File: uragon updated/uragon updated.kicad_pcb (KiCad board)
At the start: 4 copper layers, 89.7 x 62 mm, 70 parts, among them J1 USB_C_Receptacle_USB2.0_16P, J10 Conn_01x02_Socket, J11 01x07, J2 Conn_01x16_Socket, J3 Conn_01x16_Socket, J4 Conn_01x02_Socket, J5 01x07, J6 01x03, J7 01x03, J8 01x04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

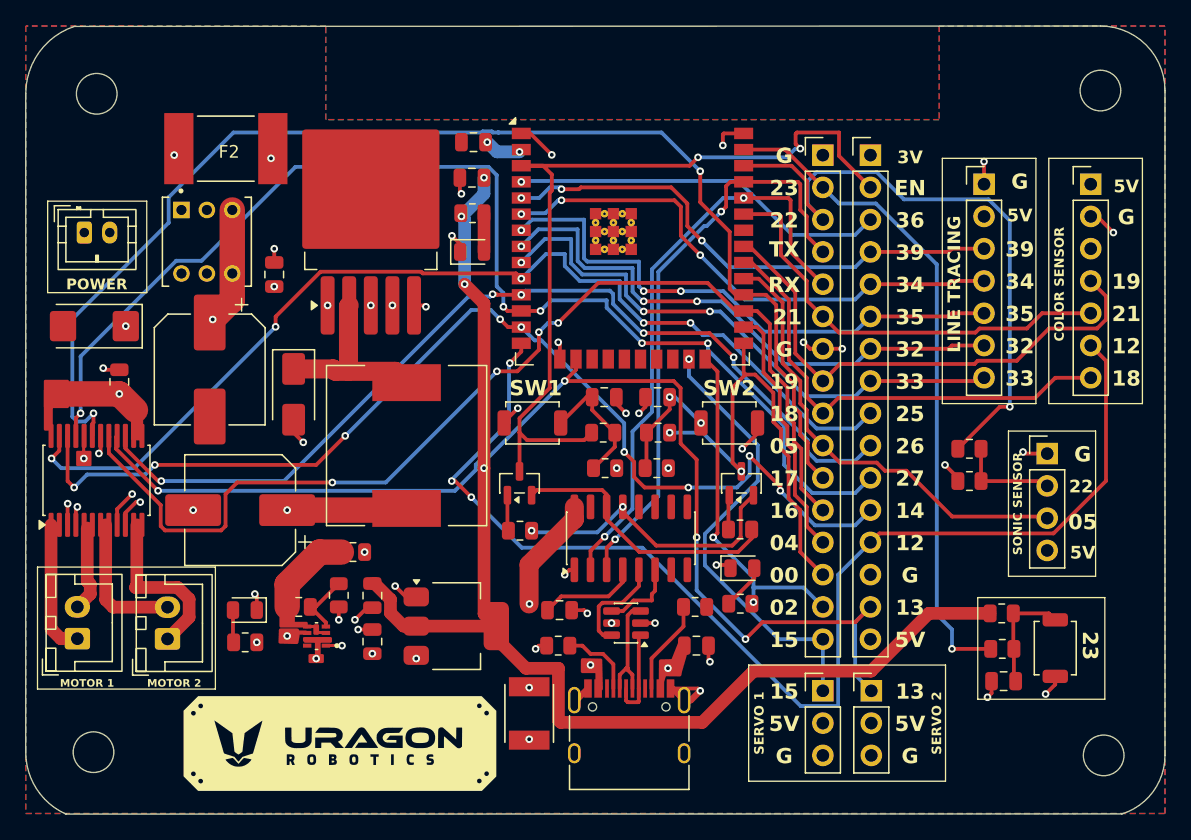
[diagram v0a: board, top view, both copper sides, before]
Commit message: Added diodes
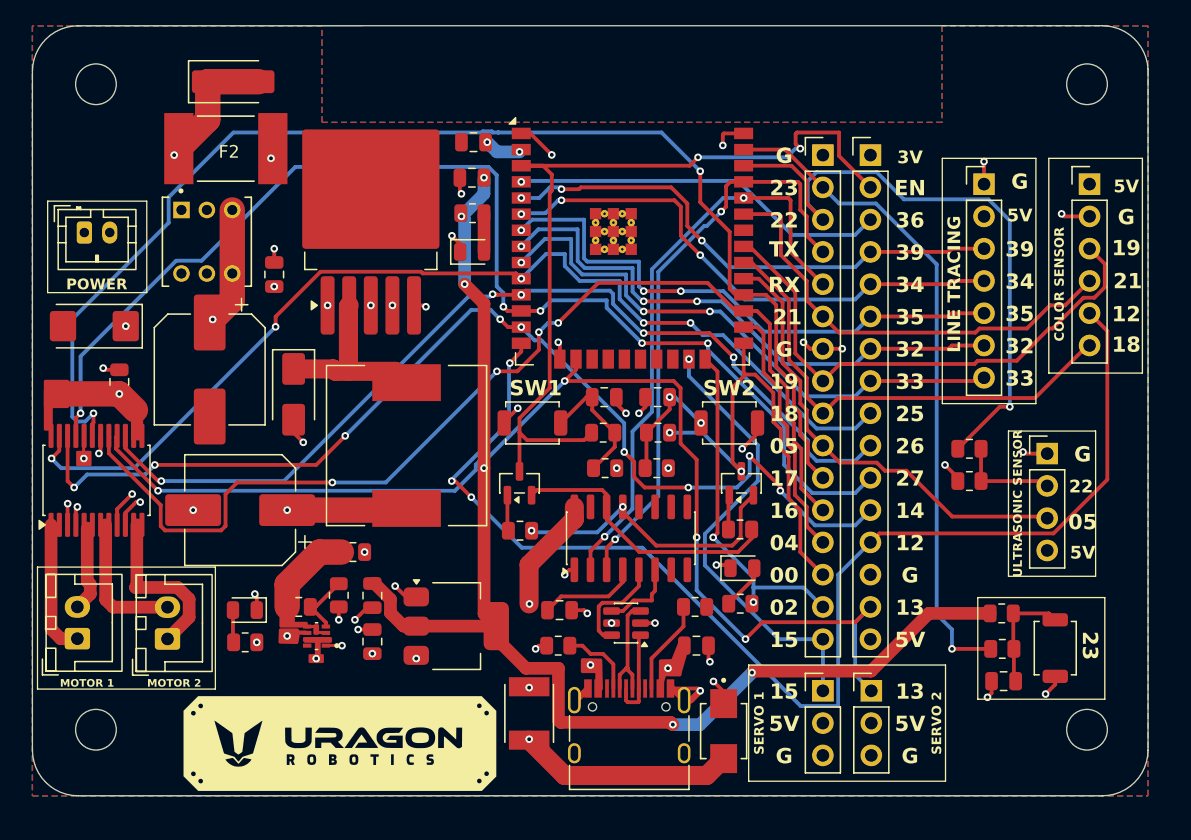
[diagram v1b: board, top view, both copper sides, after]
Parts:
- removed J11: 01x07, Connector_PinHeader_2.54mm:PinHeader_1x07_P2.54mm_Vertical
- added D5: SMBJ5.0A, SMBJ5.0A:DIOM4336X265N, F.Cu at (164.4, 107.3)
- added D6: SS54, Diode_SMD:D_SMA, F.Cu at (125.8, 56.2)
- added J12: Conn_01x06_Socket, Connector_PinHeader_2.54mm:PinHeader_1x06_P2.54mm_Vertical, F.Cu at (193.2, 64.3)
- moved H1 2.41 mm to (193.0, 107.2)
- moved H2 1.78 mm to (115.0, 107.2)
- moved H3 1.17 mm to (193.0, 56.4)
- moved H4 0.75 mm to (115.0, 56.4)
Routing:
- net +5V_USB: track 55.2 -> 72.2 mm
- net Net-(D6-A): track 9.19 -> 19.4 mm
- net GPIO12: track 96.5 -> 99.2 mm
- net GND: track 68.5 -> 70.5 mm, vias 41 -> 42
- net GPIO19: track 41.3 -> 42.2 mm
- net GPIO21: track 34.5 -> 35.4 mm
- net GPIO18: track 37.1 -> 38.0 mm
- net +3.3V: vias 8 -> 10
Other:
- board size 89.7 x 62 mm -> 87.8 x 60.6 mm
- board text added: "ULTRASONIC SENSOR"
- board text removed: "SONIC SENSOR"

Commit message: Added gitignore
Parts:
- moved H1 1.20 mm to (193.0, 108.4)
- moved H2 1.20 mm to (115.0, 108.4)
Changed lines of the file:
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@@
 	(footprint "MountingHole:MountingHole_3.2mm_M3"
 		(layer "F.Cu")
-		(at 115 107.2)
+		(at 115 108.4)
 		(descr "Mounting Hole 3.2mm, M3, no annular, generated by kicad-footprint-generator mountinghole.py")
 		(tags "mountinghole M3")
@@
 	(footprint "MountingHole:MountingHole_3.2mm_M3"
 		(layer "F.Cu")
-		(at 193 107.2)
+		(at 193 108.4)
 		(descr "Mounting Hole 3.2mm, M3, no annular, generated by kicad-footprint-generator mountinghole.py")
 		(tags "mountinghole M3")
@@
 		(min_thickness 0.25)
 		(filled_areas_thickness no)
-		(fill
+		(fill yes
 			(thermal_gap 0.5)
 			(thermal_bridge_width 0.5)

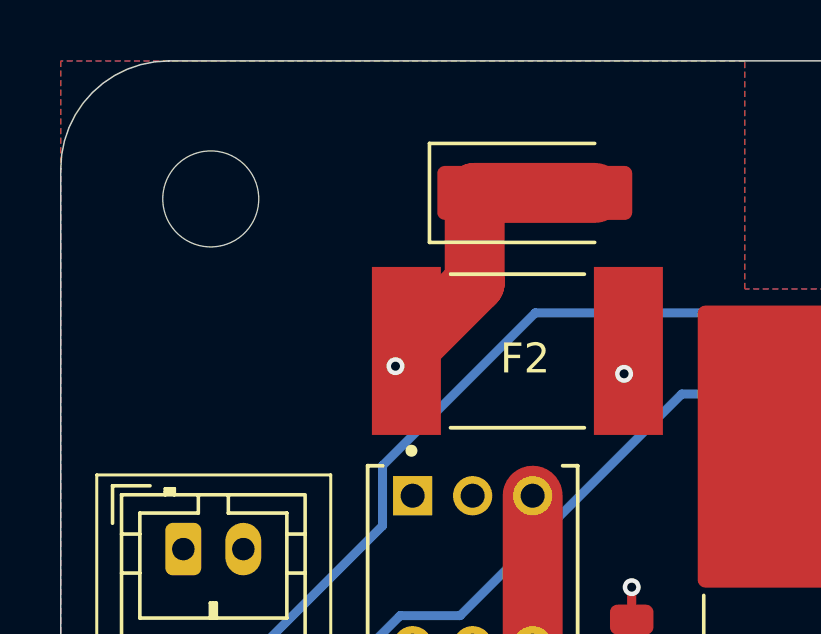
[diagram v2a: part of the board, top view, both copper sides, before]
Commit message: Changed the position of Diode_SMD:D_SMA
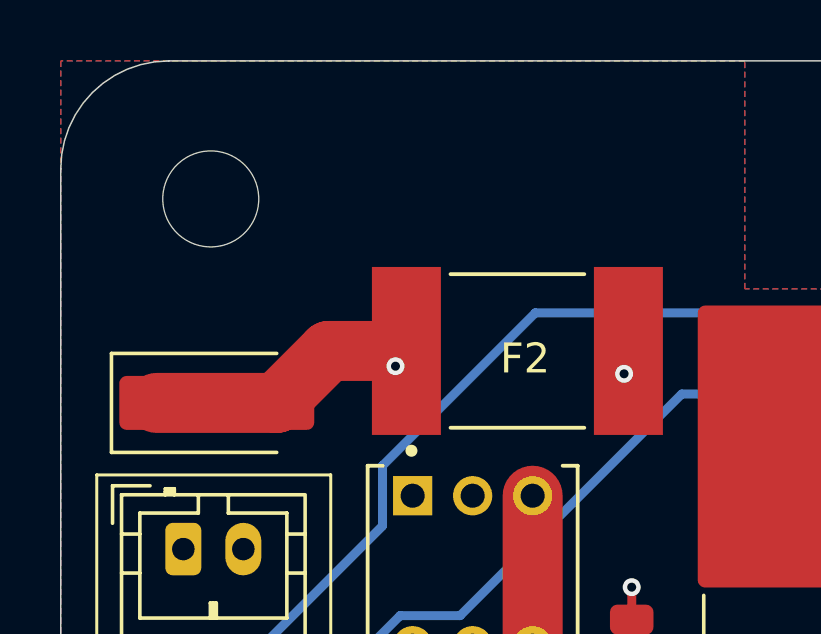
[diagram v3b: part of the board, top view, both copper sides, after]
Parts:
- moved D6 12.7 mm to (115.2, 63.2)
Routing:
- net Net-(D6-A): track 19.4 -> 18.2 mm
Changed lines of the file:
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@@
 	(footprint "Diode_SMD:D_SMA"
 		(layer "F.Cu")
-		(at 125.8 56.2)
+		(at 115.2 63.2)
 		(descr "Diode SMA (DO-214AC)")
 		(tags "Diode SMA (DO-214AC)")
@@
 	)
 	(segment
-		(start 127.8 56.2)
-		(end 123.8 56.2)
+		(start 113.2 63.2)
+		(end 117.2 63.2)
 		(width 2)
 		(layer "F.Cu")
@@
 	)
 	(segment
-		(start 123.8 59.19)
-		(end 121.522 61.468)
+		(start 121.522 61.468)
+		(end 118.932 61.468)
 		(width 2)
 		(layer "F.Cu")
@@
 	)
 	(segment
-		(start 123.8 56.2)
-		(end 123.8 59.19)
+		(start 118.932 61.468)
+		(end 117.2 63.2)
 		(width 2)
 		(layer "F.Cu")

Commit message: Fix some connections.
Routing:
- net Net-(D6-A): track 18.2 -> 15.1 mm, vias 1 -> 0
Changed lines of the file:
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@@
+	)
+	(segment
+		(start 116.086 66.086)
+		(end 113.2 63.2)
+		(width 2)
+		(layer "F.Cu")
+		(net 47)
+	)
+	(segment
+		(start 119.79 63.2)
+		(end 121.522 61.468)
+		(width 2)
+		(layer "F.Cu")
+		(net 47)
+	)
+	(segment
+		(start 116.086 68.072)
+		(end 116.086 66.086)
+		(width 2)
+		(layer "F.Cu")
+		(net 47)
 	)
 	(segment
@@
 	)
 	(segment
-		(start 121.522 61.468)
-		(end 118.932 61.468)
+		(start 117.2 63.2)
+		(end 119.79 63.2)
 		(width 2)
 		(layer "F.Cu")
 		(net 47)
 	)
-	(segment
-		(start 118.932 61.468)
-		(end 117.2 63.2)
-		(width 2)
-		(layer "F.Cu")
-		(net 47)
-	)
-	(via
-		(at 121.158 61.976)
-		(size 0.6)
-		(drill 0.3)
-		(layers "F.Cu" "B.Cu")
-		(net 47)
-	)
-	(segment
-		(start 121.158 61.976)
-		(end 121.412 61.976)
-		(width 2)
-		(layer "In2.Cu")
-		(net 47)
-	)
-	(segment
-		(start 116.086 68.072)
-		(end 116.586 67.572)
-		(width 2)
-		(layer "In2.Cu")
-		(net 47)
-	)
-	(segment
-		(start 116.586 65.278)
-		(end 119.888 61.976)
-		(width 2)
-		(layer "In2.Cu")
-		(net 47)
-	)
-	(segment
-		(start 116.586 67.572)
-		(end 116.586 65.278)
-		(width 2)
-		(layer "In2.Cu")
-		(net 47)
-	)
-	(segment
-		(start 119.888 61.976)
-		(end 121.158 61.976)
-		(width 2)
-		(layer "In2.Cu")
-		(net 47)
-	)

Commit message: Fix some connections
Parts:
- turned D6 to 180 degrees
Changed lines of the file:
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@@
 	(footprint "Diode_SMD:D_SMA"
 		(layer "F.Cu")
-		(at 115.2 63.2)
+		(at 115.2 63.2 180)
 		(descr "Diode SMA (DO-214AC)")
 		(tags "Diode SMA (DO-214AC)")
@@
 		)
 		(property "Datasheet" "~"
-			(at 0 0 0)
+			(at 0 0 180)
 			(unlocked yes)
 			(layer "F.Fab")
@@
 		)
 		(property "Description" "Schottky diode"
-			(at 0 0 0)
+			(at 0 0 180)
 			(unlocked yes)
 			(layer "F.Fab")
@@
 		(attr smd)
 		(fp_line
-			(start -3.51 -1.65)
-			(end -3.51 1.65)
+			(start -3.51 1.65)
+			(end 2 1.65)
 			(stroke
 				(width 0.12)
@@
 		)
 		(fp_line
-			(start -3.51 1.65)
-			(end 2 1.65)
+			(start -3.51 -1.65)
+			(end -3.51 1.65)
 			(stroke
 				(width 0.12)
@@
 		)
 		(fp_line
-			(start -3.5 -1.75)
-			(end 3.5 -1.75)
+			(start 3.5 1.75)
+			(end -3.5 1.75)
 			(stroke
 				(width 0.05)
@@
 		)
 		(fp_line
-			(start -3.5 1.75)
-			(end -3.5 -1.75)
+			(start 3.5 -1.75)
+			(end 3.5 1.75)
 			(stroke
 				(width 0.05)
@@
 		)
 		(fp_line
-			(start 3.5 -1.75)
-			(end 3.5 1.75)
+			(start -3.5 1.75)
+			(end -3.5 -1.75)
 			(stroke
 				(width 0.05)
@@
 		)
 		(fp_line
-			(start 3.5 1.75)
-			(end -3.5 1.75)
+			(start -3.5 -1.75)
+			(end 3.5 -1.75)
 			(stroke
 				(width 0.05)
@@
 		)
 		(fp_line
-			(start -2.3 1.5)
-			(end -2.3 -1.5)
+			(start 2.3 1.5)
+			(end -2.3 1.5)
 			(stroke
 				(width 0.1)
@@
 		)
 		(fp_line
-			(start -0.64944 -0.79908)
-			(end -0.64944 0.80112)
+			(start 2.3 -1.5)
+			(end 2.3 1.5)
 			(stroke
 				(width 0.1)
@@
 		)
 		(fp_line
-			(start -0.64944 0.00102)
-			(end -1.55114 0.00102)
+			(start 2.3 -1.5)
+			(end -2.3 -1.5)
 			(stroke
 				(width 0.1)
@@
 		)
 		(fp_line
-			(start -0.64944 0.00102)
+			(start 0.50118 0.75032)
 			(end 0.50118 -0.79908)
 			(stroke
@@
 		)
 		(fp_line
-			(start -0.64944 0.00102)
-			(end 0.50118 0.75032)
+			(start 0.50118 0.00102)
+			(end 1.4994 0.00102)
 			(stroke
 				(width 0.1)
@@
 		)
 		(fp_line
-			(start 0.50118 0.00102)
-			(end 1.4994 0.00102)
+			(start -0.64944 0.00102)
+			(end 0.50118 0.75032)
 			(stroke
 				(width 0.1)
@@
 		)
 		(fp_line
-			(start 0.50118 0.75032)
+			(start -0.64944 0.00102)
 			(end 0.50118 -0.79908)
 			(stroke
@@
 		)
 		(fp_line
-			(start 2.3 -1.5)
-			(end -2.3 -1.5)
+			(start -0.64944 0.00102)
+			(end -1.55114 0.00102)
 			(stroke
 				(width 0.1)
@@
 		)
 		(fp_line
-			(start 2.3 -1.5)
-			(end 2.3 1.5)
+			(start -0.64944 -0.79908)
+			(end -0.64944 0.80112)
 			(stroke
 				(width 0.1)
@@
 		)
 		(fp_line
-			(start 2.3 1.5)
-			(end -2.3 1.5)
+			(start -2.3 1.5)
+			(end -2.3 -1.5)
 			(stroke
 				(width 0.1)
@@
 		)
 		(pad "1" smd roundrect
-			(at -2 0)
+			(at -2 0 180)
 			(size 2.5 1.8)
 			(layers "F.Cu" "F.Mask" "F.Paste")
@@
 		)
 		(pad "2" smd roundrect
-			(at 2 0)
+			(at 2 0 180)
 			(size 2.5 1.8)
 			(layers "F.Cu" "F.Mask" "F.Paste")
@@
 	)
 	(segment
-		(start 116.086 66.086)
-		(end 113.2 63.2)
+		(start 116.086 68.072)
+		(end 116.086 66.086)
 		(width 2)
 		(layer "F.Cu")
@@
 	)
 	(segment
-		(start 116.086 68.072)
-		(end 116.086 66.086)
+		(start 113.2 63.2)
+		(end 117.2 63.2)
 		(width 2)
 		(layer "F.Cu")
@@
 	)
 	(segment
-		(start 113.2 63.2)
-		(end 117.2 63.2)
+		(start 117.2 63.2)
+		(end 119.79 63.2)
 		(width 2)
 		(layer "F.Cu")
@@
 	)
 	(segment
-		(start 117.2 63.2)
-		(end 119.79 63.2)
+		(start 116.086 66.086)
+		(end 113.2 63.2)
 		(width 2)
 		(layer "F.Cu")
